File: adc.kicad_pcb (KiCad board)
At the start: 2 copper layers, 17 parts, among them U701 ADS8665IPWR

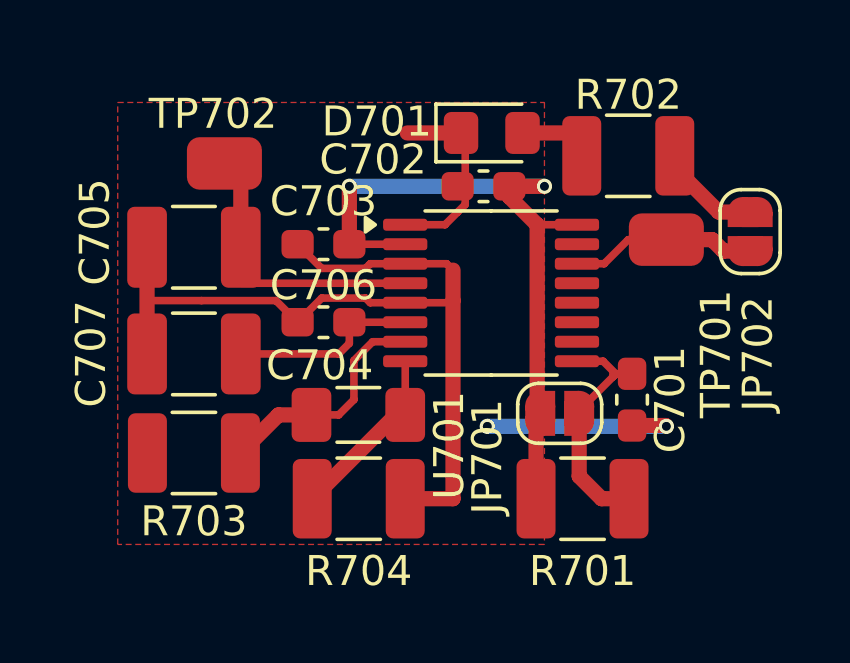
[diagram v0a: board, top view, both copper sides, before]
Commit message: edit silkscreen
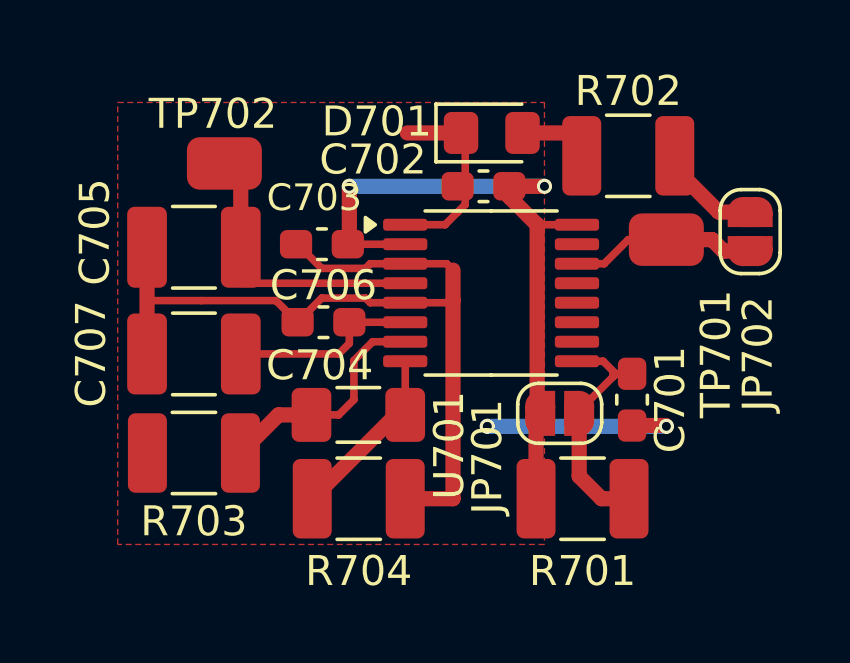
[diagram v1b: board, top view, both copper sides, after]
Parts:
- moved C703 0.05 mm to (69.5, 55.8)
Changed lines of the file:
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@@
 		)
 		(property "Value" "SolderJumper_2_Open"
-			(at 0 1.9 360)
+			(at 0 1.9 0)
 			(layer "F.Fab")
 			(effects
@@
 		(tags "capacitor handsolder")
 		(property "Reference" "C702"
-			(at -3.683 -0.889 360)
+			(at -3.683 -0.889 0)
 			(layer "F.SilkS")
 			(effects
@@
 		)
 		(property "Value" "1u"
-			(at 0 1.43 360)
+			(at 0 1.43 0)
 			(layer "F.Fab")
 			(effects
@@
 		)
 		(fp_text user "${REFERENCE}"
-			(at 0 0 360)
+			(at 0 0 0)
 			(layer "F.Fab")
 			(effects
@@
 		(tags "LED handsolder")
 		(property "Reference" "D701"
-			(at -3.8325 -0.381 360)
+			(at -3.8325 -0.381 0)
 			(layer "F.SilkS")
 			(effects
@@
 		)
 		(property "Value" "LED"
-			(at 0 1.65 360)
+			(at 0 1.65 0)
 			(layer "F.Fab")
 			(effects
@@
 		)
 		(fp_text user "${REFERENCE}"
-			(at 0 0 360)
+			(at 0 0 0)
 			(layer "F.Fab")
 			(effects
@@
 	(footprint "meas:C_0603_1608Metric_Pad1.08x0.95mm_HandSolder"
 		(layer "F.Cu")
-		(at 69.596 55.779)
+		(at 69.5452 55.7784)
 		(descr "Capacitor SMD 0603 (1608 Metric), square (rectangular) end terminal, IPC_7351 nominal with elongated pad for handsoldering. (Body size source: IPC-SM-782 page 76, https://www.pcb-3d.com/wordpress/wp-content/uploads/ipc-sm-782a_amendment_1_and_2.pdf), generated with kicad-footprint-generator")
 		(tags "capacitor handsolder")
 		(property "Reference" "C703"
-			(at 0 -1.43 360)
+			(at -0.254 -1.55 0)
 			(layer "F.SilkS")
 			(effects
 				(font
-					(size 1 1)
+					(size 0.889 0.889)
 					(thickness 0.15)
 				)
@@
 		)
 		(property "Value" "1u"
-			(at 0 1.43 360)
+			(at 0 1.43 0)
 			(layer "F.Fab")
 			(effects
@@
 		)
 		(fp_text user "${REFERENCE}"
-			(at 0 0 360)
+			(at 0 0 0)
 			(layer "F.Fab")
 			(effects
@@
 		(tags "resistor handsolder")
 		(property "Reference" "R701"
-			(at 0 2.413 360)
+			(at 0 2.413 0)
 			(layer "F.SilkS")
 			(effects
@@
 		)
 		(property "Value" "1k"
-			(at 0 2.28 360)
+			(at 0 2.28 0)
 			(layer "F.Fab")
 			(effects
@@
 		)
 		(fp_text user "${REFERENCE}"
-			(at 0 0 360)
+			(at 0 0 0)
 			(layer "F.Fab")
 			(effects
@@
 		)
 		(property "Value" "ADS8665IPWR"
-			(at 0 3.45 360)
+			(at 0 3.45 0)
 			(layer "F.Fab")
 			(effects
@@
 		)
 		(fp_text user "${REFERENCE}"
-			(at 0 0 360)
+			(at 0 0 0)
 			(layer "F.Fab")
 			(effects
@@
 		)
 		(property "Value" "~"
-			(at 0 1.65 360)
+			(at 0 1.65 0)
 			(layer "F.Fab")
 			(effects
@@
 		)
 		(fp_text user "${REFERENCE}"
-			(at 0 0 360)
+			(at 0 0 0)
 			(layer "F.Fab")
 			(effects
@@
 		(tags "resistor handsolder")
 		(property "Reference" "R702"
-			(at 0 2.032 180)
+			(at 0 2.159 180)
 			(layer "F.SilkS")
 			(effects
@@
 		)
 		(property "Value" "10u"
-			(at 0 2.3 360)
+			(at 0 2.3 0)
 			(layer "F.Fab")
 			(effects
@@
 		)
 		(fp_text user "${REFERENCE}"
-			(at 0 0 360)
+			(at 0 0 0)
 			(layer "F.Fab")
 			(effects
@@
 		(tags "resistor")
 		(property "Reference" "TP702"
-			(at -0.381 -1.651 360)
+			(at -0.381 -1.651 0)
 			(layer "F.SilkS")
 			(effects
@@
 		)
 		(property "Value" "~"
-			(at 0 1.65 360)
+			(at 0 1.65 0)
 			(layer "F.Fab")
 			(effects
@@
 		)
 		(fp_text user "${REFERENCE}"
-			(at 0 0 360)
+			(at 0 0 0)
 			(layer "F.Fab")
 			(effects
@@
 		)
 		(property "Value" "10u"
-			(at 0 2.3 360)
+			(at 0 2.3 0)
 			(layer "F.Fab")
 			(effects
@@
 		)
 		(fp_text user "${REFERENCE}"
-			(at 0 0 360)
+			(at 0 0 0)
 			(layer "F.Fab")
 			(effects
@@
 		(tags "resistor handsolder")
 		(property "Reference" "R704"
-			(at 0 2.413 360)
+			(at 0 2.413 0)
 			(layer "F.SilkS")
 			(effects
@@
 		)
 		(property "Value" "100"
-			(at 0 2.28 360)
+			(at 0 2.28 0)
 			(layer "F.Fab")
 			(effects
@@
 		)
 		(fp_text user "${REFERENCE}"
-			(at 0 0 360)
+			(at 0 0 0)
 			(layer "F.Fab")
 			(effects
@@
 		(tags "capacitor handsolder")
 		(property "Reference" "C706"
-			(at 0 -1.229 360)
+			(at 0 -1.229 0)
 			(layer "F.SilkS")
 			(effects
@@
 		)
 		(property "Value" "1u"
-			(at 0 1.43 360)
+			(at 0 1.43 0)
 			(layer "F.Fab")
 			(effects
@@
 		)
 		(fp_text user "${REFERENCE}"
-			(at 0 0 360)
+			(at 0 0 0)
 			(layer "F.Fab")
 			(effects
